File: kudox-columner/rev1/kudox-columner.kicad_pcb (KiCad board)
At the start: 2 copper layers, 146 x 132.3 mm, 85 parts, among them K0 KEYSW, K1 KEYSW, K10 KEYSW, K11 KEYSW, K12 KEYSW, K13 KEYSW, K14 KEYSW, K15 KEYSW, K16 KEYSW, K2 KEYSW, K20 KEYSW, K21 KEYSW, K22 KEYSW, K23 KEYSW, K24 KEYSW, K25 KEYSW, K3 KEYSW, K30 KEYSW, K31 KEYSW, K32 KEYSW, K33 KEYSW, K34 KEYSW, K35 KEYSW, K4 KEYSW, K40 KEYSW, K41 KEYSW, K42 KEYSW, K43 KEYSW, K44 KEYSW, K45 KEYSW, K46 KEYSW, K5 KEYSW, K6 KEYSW, U1 ProMicro

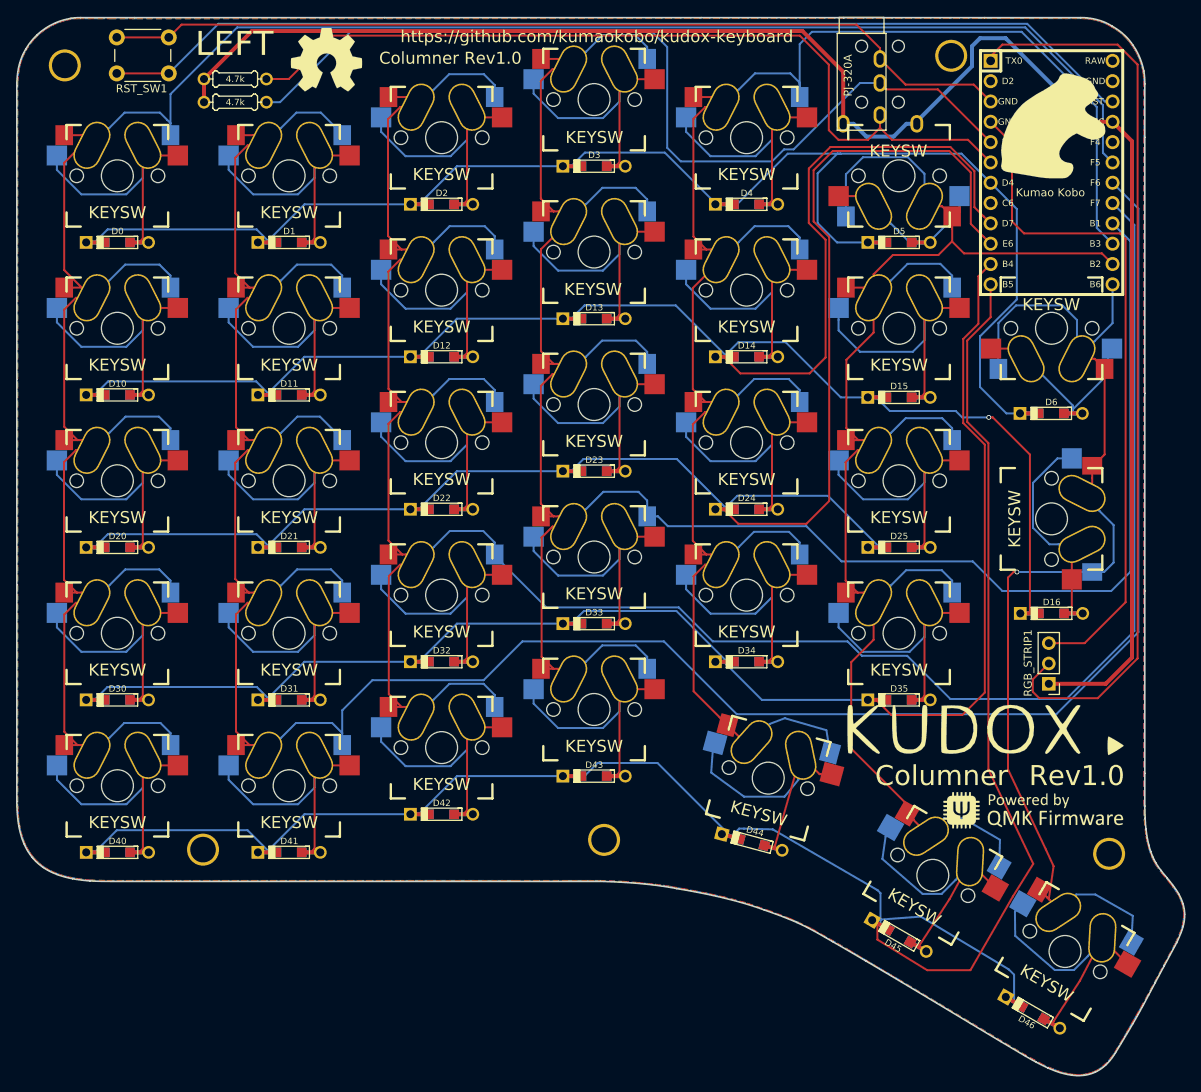
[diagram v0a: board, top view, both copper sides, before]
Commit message: Modify footprints of switches on kudox-columner
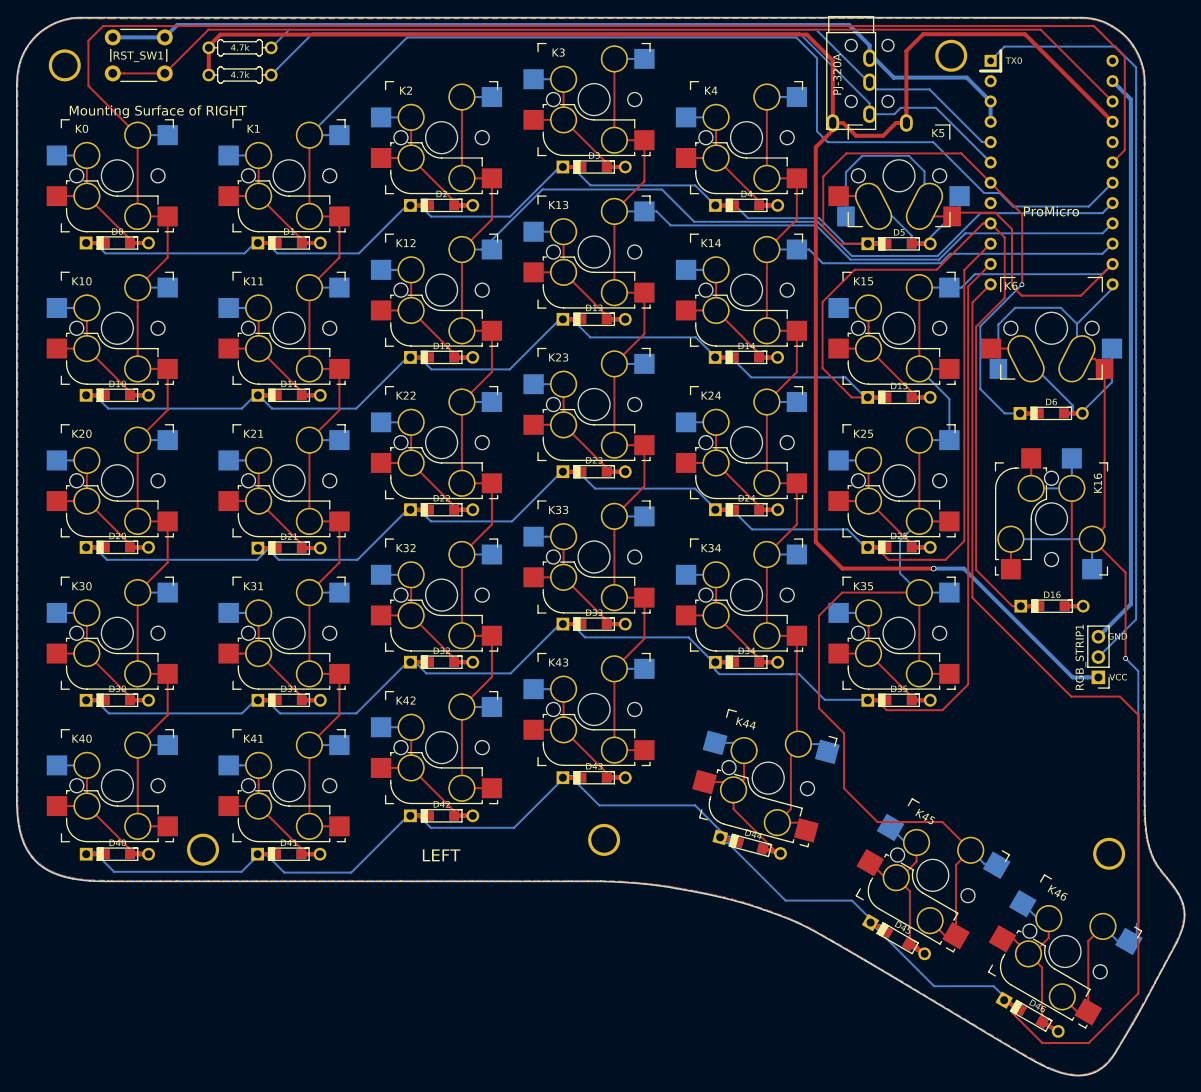
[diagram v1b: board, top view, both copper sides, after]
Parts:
- removed -3, REF***: OSHW-Logo2_14.6x12mm_SilkScreen, Symbols:OSHW-Symbol_8.9x8mm_SilkScreen
- removed the G*** at (209.5, 44.6)
- removed the G*** at (206.5, 130.2)
- added G***: LOGO, kudox_footprints:kumao-icon-left-pad, B.Cu at (209.4, 47.5)
- added G***: LOGO, kudox_footprints:qmk-badge-pad, B.Cu at (208.5, 130.3)
- added G***: kudox_github, kudox_footprints:kudox_github, F.Cu at (81.9, 84.0)
- added G***: kudox_github, kudox_footprints:kudox_github, B.Cu at (81.9, 84.0)
- added G***: LOGO, kudox_footprints:columner_version, B.Cu at (203.2, 125.8)
- added G***: LOGO, kudox_footprints:columner_version, F.Cu at (203.2, 125.8)
- G***: value kumao-icon-right -> LOGO; footprint kudox_footprints:kumao-icon-right -> kudox_footprints:kumao-icon-right-pad
- G***: footprint myparts:qmk-badge -> kudox_footprints:qmk-badge-pad
- G***: footprint kudox_footprints:kudox-logo -> kudox_footprints:kudox-logo-pad
- K0, K1, K10, K11, K12, K13, K14, K15, K2, K20, K21, K22, K23, K24, K25, K3, K30, K31, K32, K33, K34, K35, K4, K40, K41, K42, K43, K44, K45, K46: footprint kudox_footprints:Mx_hotswappable -> kudox_footprints:MX_reversible_100
- K16: footprint kudox_footprints:Mx_hotswappable_125 -> kudox_footprints:MX_reversible_100
- K6: footprint kudox_footprints:Mx_hotswappable_125 -> kudox_footprints:Mx_hotswappable
- RGB_STRIP1: footprint kudox_footprints:Pin_Header_Straight_1x03_Pitch2.54mm -> kudox_footprints:RGB-Strip
- e: renamed from G***; footprint kudox_footprints:kudox-logo -> kudox_footprints:kudox-logo-pad
- moved R1 6.83 mm to (107.9, 34.8)
- moved RGB_STRIP1 6.25 mm to (215.2, 113.5)
- moved G*** 3.82 mm to (209.4, 47.5)
- moved G*** 3.46 mm to (204.4, 121.0)
- moved e 2.03 mm to (202.0, 121.0)
- moved G*** 1.42 mm to (208.5, 130.3)
- moved TRRS1 1.30 mm to (186.6, 32.9)
- moved D16 0.90 mm to (209.4, 104.6)
- moved R2 0.78 mm to (107.9, 38.2)
- moved RST_SW1 0.50 mm to (98.5, 38.0)
- moved D44 0.45 mm to (171.7, 134.5)
- moved D46 0.45 mm to (206.8, 155.8)
- moved D45 0.36 mm to (190.1, 146.1)
- moved D41 0.23 mm to (114.0, 135.6)
- moved D40 0.23 mm to (92.6, 135.6)
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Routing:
- net col2: track 318.2 -> 217.7 mm
- net col1: track 342.3 -> 250.9 mm
- net col3: track 281.4 -> 193.0 mm
- net col4: track 240.7 -> 175.8 mm
- net row2: track 210.5 -> 172.1 mm
- net row4: track 252.5 -> 273.1 mm
- net col5: track 206.8 -> 227.4 mm
- net row1: track 235.0 -> 215.3 mm, vias 1 -> 0
- net Net-(D15-Pad2): track 40.6 -> 21.6 mm
- net rgb_data: track 114.7 -> 95.7 mm
- net col0: track 309.1 -> 290.2 mm
- net SDA: track 115.4 -> 96.7 mm
- net VCC: track 219.0 -> 237.6 mm
- net Net-(D14-Pad2): track 36.0 -> 21.5 mm
- net Net-(D20-Pad2): track 36.0 -> 21.5 mm
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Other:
- board text added: "Mounting Surface of LEFT"
- board text added: "Mounting Surface of RIGHT"
- board text removed: "Columner"
- board text removed: "Columner Rev1.0"
- board text removed: "Kumao Kobo"
- board text removed: "Rev1.0"
- board text removed: "https://github.com/kumaokobo/kudox-keyboard"

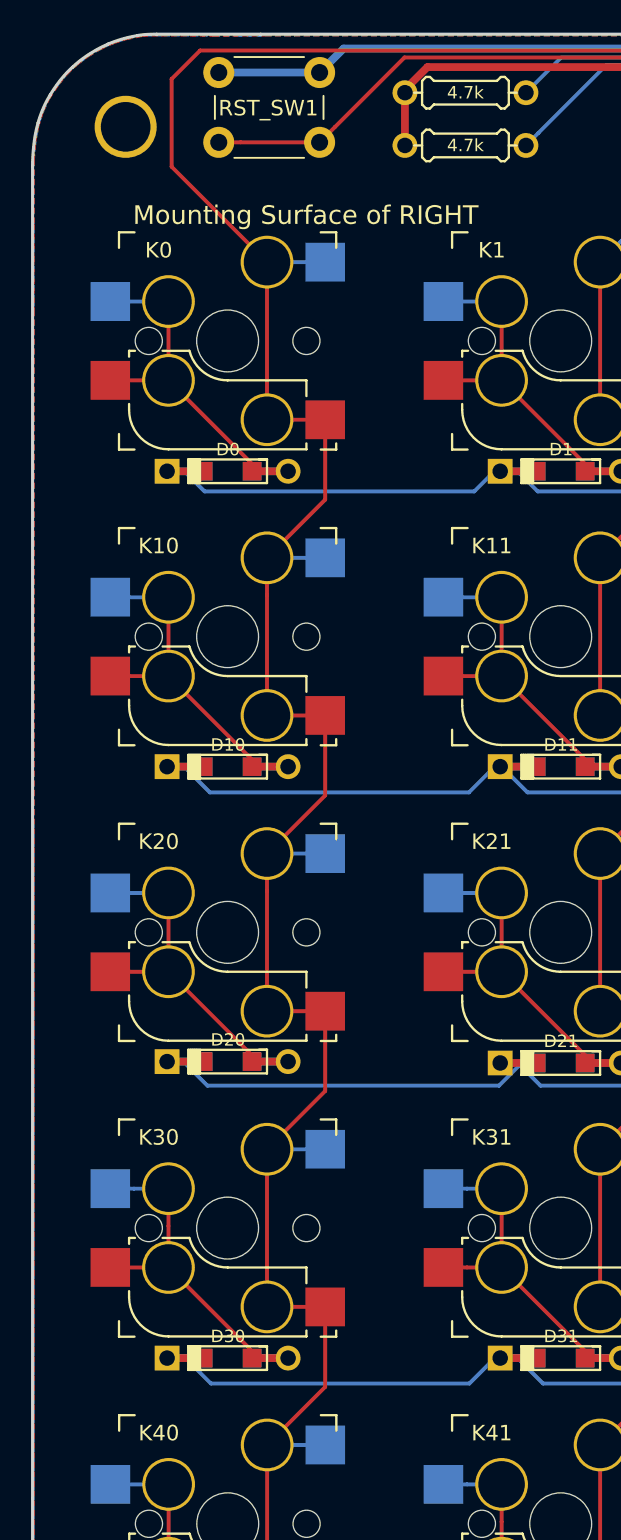
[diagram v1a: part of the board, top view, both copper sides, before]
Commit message: Modify kudox-columner to add RGB pad
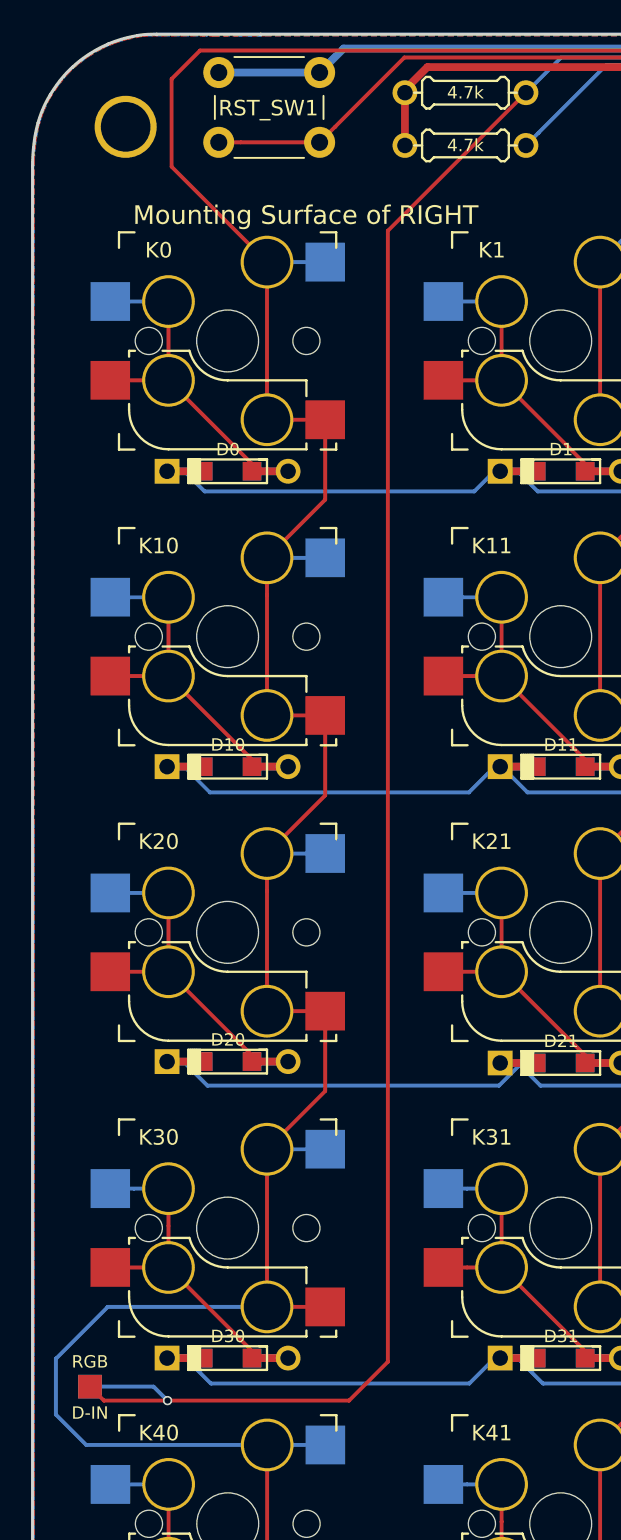
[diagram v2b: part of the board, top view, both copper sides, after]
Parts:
- added J1: RGB, kudox_footprints:pad_1x1, F.Cu at (83.7, 118.2)
- added J2: RGB, kudox_footprints:pad_1x1, B.Cu at (83.7, 118.2)
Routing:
- net SDA: track 96.7 -> 208.2 mm, vias 0 -> 1
- net col0: track 290.2 -> 312.8 mm
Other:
- board text added: "D-IN"
- board text added: "D-OUT"
